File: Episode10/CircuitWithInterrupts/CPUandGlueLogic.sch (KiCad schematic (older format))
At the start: 27 parts, among them SW100 SW_Push, U100 74HCT245, U101 74HCT245, U102 MAX708, U103 HD6809, U104 74HCT245, U105 74HCT365, U106 74HCT00, U107 74HCT27, U108 74HCT138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

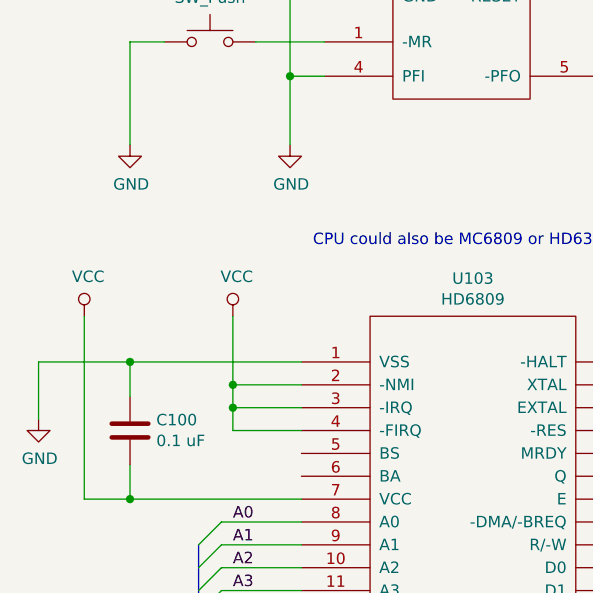
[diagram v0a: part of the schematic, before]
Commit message: integrated interrupt controller
Added ~IRQ input to core module, and changed the
wiring of the CPU's ~IRQ input to feed in the ~IRQ
output of the interrupt controller.  (A pull-up
resistor will keep this input high when the interrupt
controller isn't installed.)

Have the peripheral module send the Timer 1 output
to the interrupt controller's ~IRQ3 input.  This will
be the system periodic timer interrupt.

Also have the peripheral module export the pins of
Port C, and use PC0 and PC1 to clear the flip flops
that latch a pulse on ~IRQ3 and ~IRQ6, which are
edge-triggered.
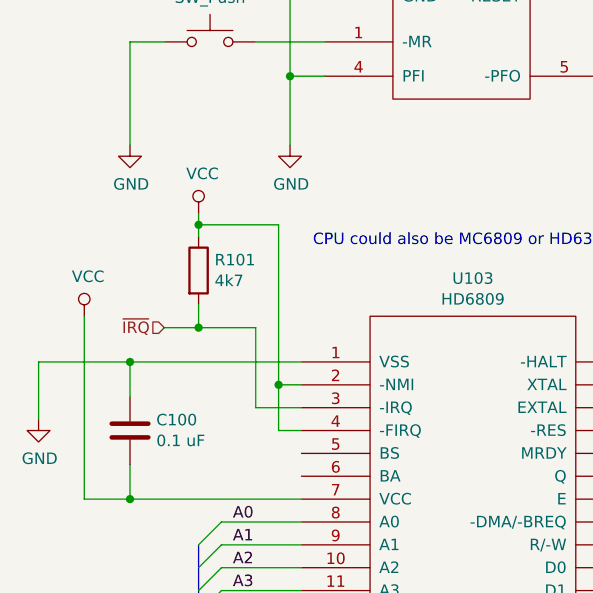
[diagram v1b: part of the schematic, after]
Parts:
- added R101: 4k7, symbol device:R
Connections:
- net labels added: ~IRQ
- wire segments 322 -> 328
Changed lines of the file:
@@
 $EndComp
 Wire Wire Line
-	1800 3750 1500 3750
-Wire Wire Line
-	1500 3750 1500 3650
-$Comp
-L power:VCC #PWR0105
-U 1 1 5CFA91DE
-P 1500 3250
-F 0 "#PWR0105" H 1500 3100 50  0001 C CNN
-F 1 "VCC" H 1517 3423 50  0000 C CNN
-F 2 "" H 1500 3250 50  0001 C CNN
-F 3 "" H 1500 3250 50  0001 C CNN
-	1    1500 3250
-	1    0    0    -1
-$EndComp
+	1800 3750 1700 3750
 Wire Wire Line
 	3300 3650 4350 3650
@@
 Connection ~ 4350 3150
 Wire Wire Line
-	1800 3650 1500 3650
-Connection ~ 1500 3650
-Wire Wire Line
-	1500 3650 1500 3550
-Wire Wire Line
-	1800 3550 1500 3550
-Connection ~ 1500 3550
-Wire Wire Line
-	1500 3550 1500 3250
+	1800 3550 1700 3550
+Connection ~ 1700 3550
 Text Notes 4000 2800 0    50   ~ 0
 Crystal frequency should be between 2 and 4 MHz.\nI used 3.6864 MHz.
@@
 Text HLabel 6850 7150 2    50   Output ~ 0
 R~W
+Wire Wire Line
+	1700 3550 1700 3750
+Wire Wire Line
+	1800 3650 1600 3650
+Wire Wire Line
+	1600 3650 1600 3300
+Wire Wire Line
+	1600 3300 1350 3300
+Text HLabel 1200 3300 0    50   Input ~ 0
+~IRQ
+$Comp
+L device:R R101
+U 1 1 5E301027
+P 1350 3050
+F 0 "R101" H 1420 3096 50  0000 L CNN
+F 1 "4k7" H 1420 3005 50  0000 L CNN
+F 2 "" V 1280 3050 50  0001 C CNN
+F 3 "" H 1350 3050 50  0001 C CNN
+	1    1350 3050
+	1    0    0    -1
+$EndComp
+Wire Wire Line
+	1350 3200 1350 3300
+Connection ~ 1350 3300
+Wire Wire Line
+	1350 3300 1200 3300
+Wire Wire Line
+	1350 2900 1350 2850
+$Comp
+L power:VCC #PWR?
+U 1 1 5E36696F
+P 1350 2800
+F 0 "#PWR?" H 1350 2650 50  0001 C CNN
+F 1 "VCC" H 1367 2973 50  0000 C CNN
+F 2 "" H 1350 2800 50  0001 C CNN
+F 3 "" H 1350 2800 50  0001 C CNN
+	1    1350 2800
+	1    0    0    -1
+$EndComp
+Wire Wire Line
+	1700 2850 1350 2850
+Wire Wire Line
+	1700 2850 1700 3550
+Connection ~ 1350 2850
+Wire Wire Line
+	1350 2850 1350 2800
 Wire Bus Line
-	1000 5700 3650 5700
+	2450 6150 2450 9200
+Wire Bus Line
+	4500 4450 4500 7250
+Wire Bus Line
+	1350 4250 1350 5600
 Wire Bus Line
 	3750 5250 3750 5600
 Wire Bus Line
-	1350 4250 1350 5600
-Wire Bus Line
-	4500 4450 4500 7250
-Wire Bus Line
-	2450 6150 2450 9200
+	1000 5700 3650 5700
 $EndSCHEMATC

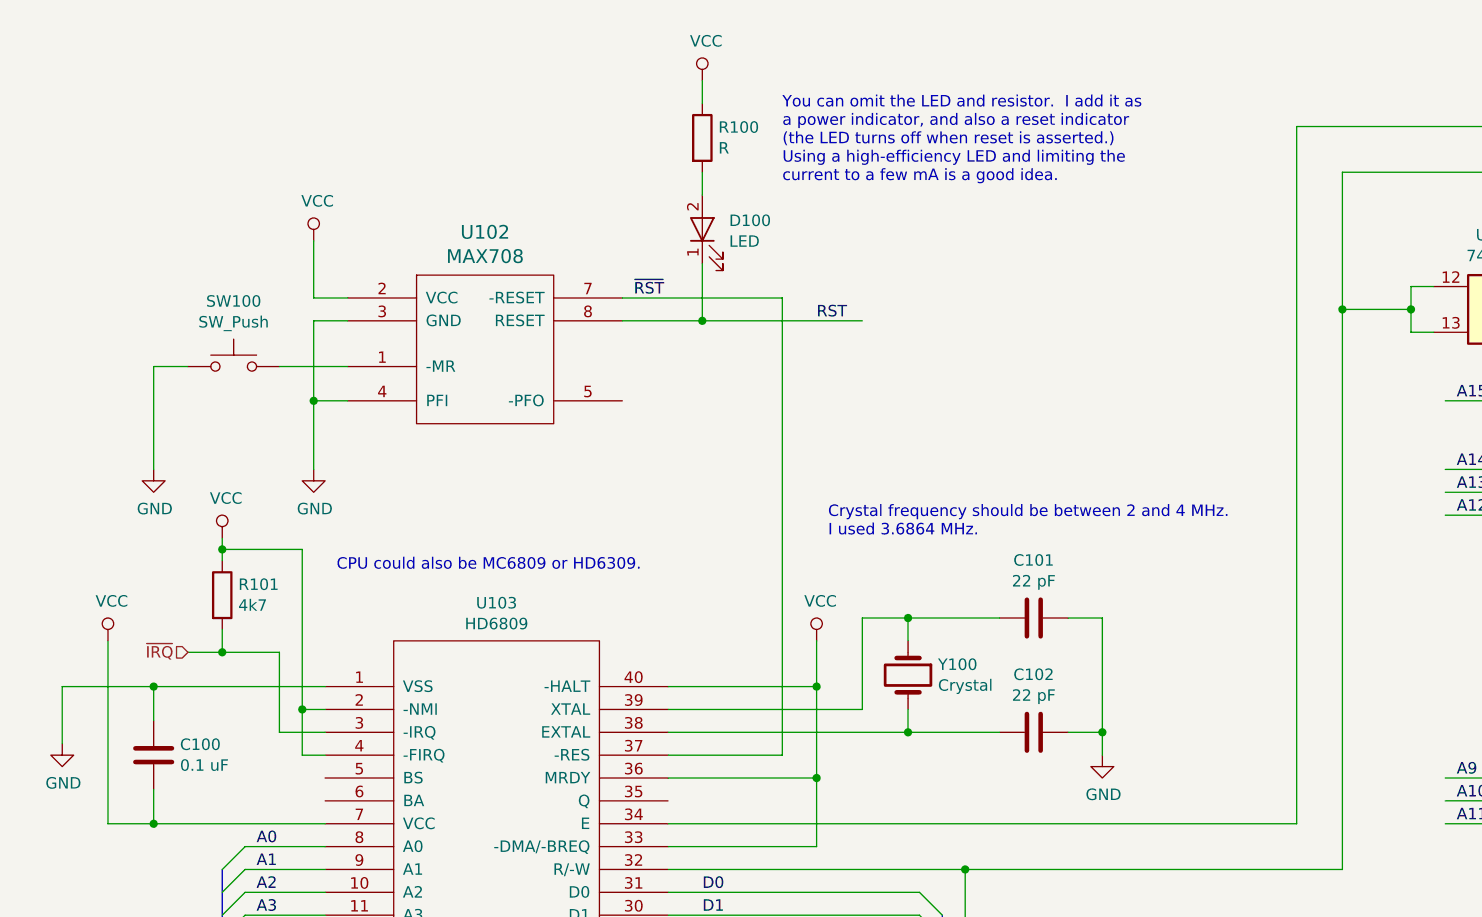
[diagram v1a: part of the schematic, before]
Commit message: add pull-ups to -IRQ, -FIRQ, and -NMI
This allows them to be driven low if used, but still
works if they are not explicitly driven.
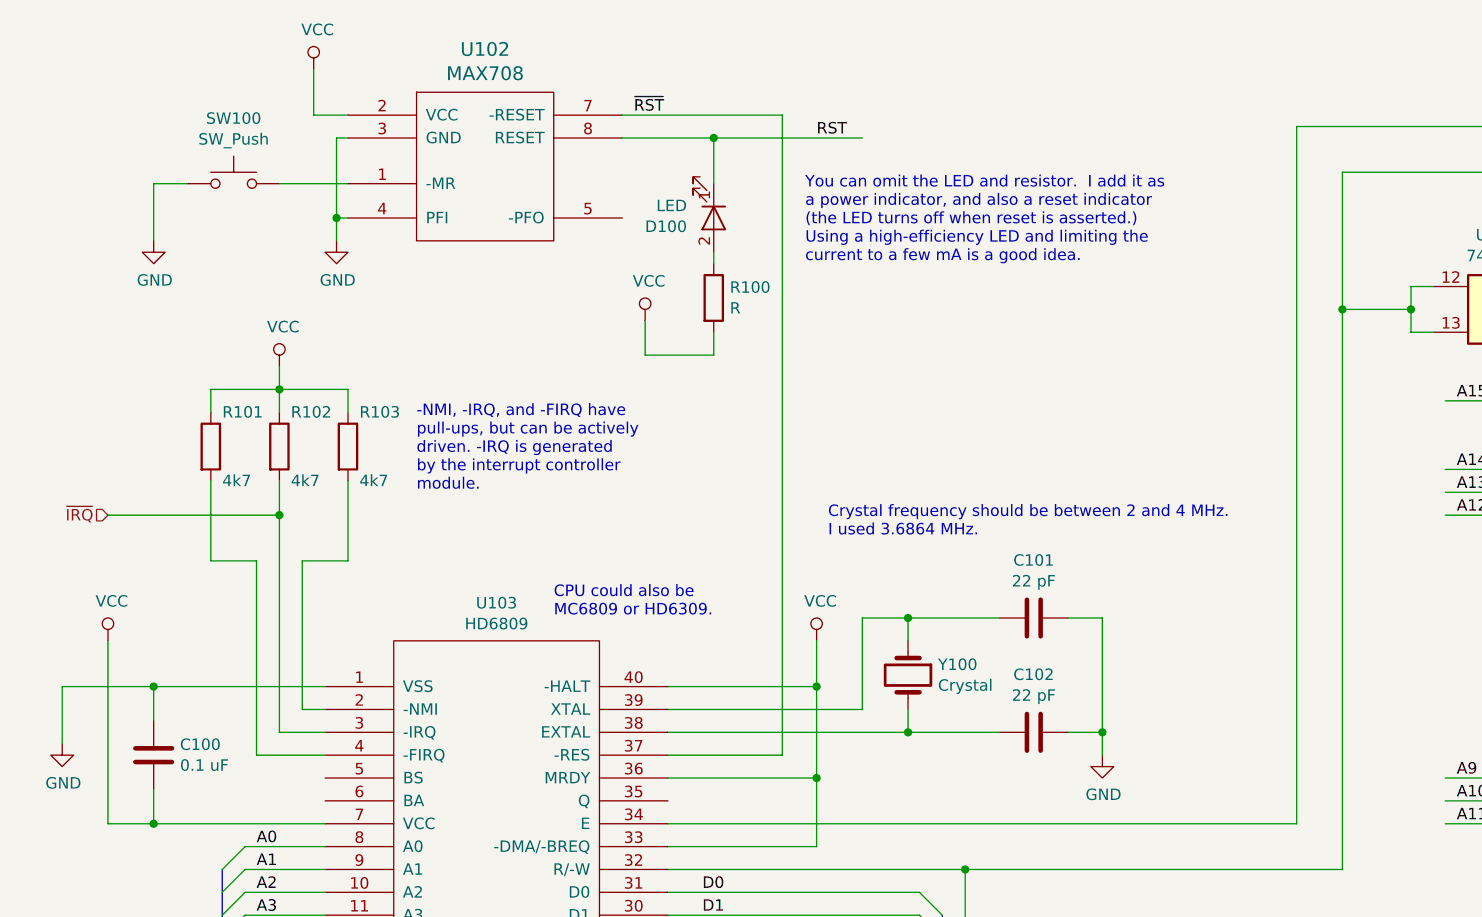
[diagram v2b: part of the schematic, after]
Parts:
- added R102, R103: 4k7, symbol device:R
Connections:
- wire segments 328 -> 336
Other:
- note added: "-NMI, -IRQ, and -FIRQ have\npull-ups, but can be actively\ndriven. -IRQ is generated\nby the interrupt controller\nmodule."
- note added: "CPU could also be\nMC6809 or HD6309."
- note removed: "CPU could also be MC6809 or HD6309."
- moved on the sheet: D100, R100, R101, SW100, U102
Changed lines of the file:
@@
 L ya68k:MAX708 U102
 U 1 1 5CFA9144
-P 2500 1950
-F 0 "U102" H 2500 2437 60  0000 C CNN
-F 1 "MAX708" H 2500 2331 60  0000 C CNN
-F 2 "" H 2500 1950 60  0000 C CNN
-F 3 "" H 2500 1950 60  0000 C CNN
-	1    2500 1950
+P 2500 1150
+F 0 "U102" H 2500 1637 60  0000 C CNN
+F 1 "MAX708" H 2500 1531 60  0000 C CNN
+F 2 "" H 2500 1150 60  0000 C CNN
+F 3 "" H 2500 1150 60  0000 C CNN
+	1    2500 1150
 	1    0    0    -1
 $EndComp
@@
 L Switch:SW_Push SW100
 U 1 1 5CFA914B
-P 1400 2050
-F 0 "SW100" H 1400 2335 50  0000 C CNN
-F 1 "SW_Push" H 1400 2244 50  0000 C CNN
-F 2 "" H 1400 2250 50  0001 C CNN
-F 3 "" H 1400 2250 50  0001 C CNN
-	1    1400 2050
-	1    0    0    -1
-$EndComp
-Wire Wire Line
-	1900 1750 1750 1750
-Wire Wire Line
-	1750 1750 1750 1500
+P 1400 1250
+F 0 "SW100" H 1400 1535 50  0000 C CNN
+F 1 "SW_Push" H 1400 1444 50  0000 C CNN
+F 2 "" H 1400 1450 50  0001 C CNN
+F 3 "" H 1400 1450 50  0001 C CNN
+	1    1400 1250
+	1    0    0    -1
+$EndComp
+Wire Wire Line
+	1900 950  1750 950
+Wire Wire Line
+	1750 950  1750 750
 $Comp
 L power:VCC #PWR0106
 U 1 1 5CFA9154
-P 1750 1500
-F 0 "#PWR0106" H 1750 1350 50  0001 C CNN
-F 1 "VCC" H 1767 1673 50  0000 C CNN
-F 2 "" H 1750 1500 50  0001 C CNN
-F 3 "" H 1750 1500 50  0001 C CNN
-	1    1750 1500
-	1    0    0    -1
-$EndComp
-Wire Wire Line
-	1900 1850 1750 1850
-Wire Wire Line
-	1750 1850 1750 2200
-Wire Wire Line
-	1900 2200 1750 2200
-Connection ~ 1750 2200
-Wire Wire Line
-	1750 2200 1750 2500
+P 1750 750
+F 0 "#PWR0106" H 1750 600 50  0001 C CNN
+F 1 "VCC" H 1767 923 50  0000 C CNN
+F 2 "" H 1750 750 50  0001 C CNN
+F 3 "" H 1750 750 50  0001 C CNN
+	1    1750 750
+	1    0    0    -1
+$EndComp
+Wire Wire Line
+	1900 1050 1850 1050
+Wire Wire Line
+	1850 1050 1850 1400
+Wire Wire Line
+	1900 1400 1850 1400
+Connection ~ 1850 1400
+Wire Wire Line
+	1850 1400 1850 1500
 $Comp
 L power:GND #PWR0107
 U 1 1 5CFA915F
-P 1750 2500
-F 0 "#PWR0107" H 1750 2250 50  0001 C CNN
-F 1 "GND" H 1755 2327 50  0000 C CNN
-F 2 "" H 1750 2500 50  0001 C CNN
-F 3 "" H 1750 2500 50  0001 C CNN
-	1    1750 2500
-	1    0    0    -1
-$EndComp
-Wire Wire Line
-	1900 2050 1600 2050
-Wire Wire Line
-	1200 2050 1050 2050
-Wire Wire Line
-	1050 2050 1050 2500
+P 1850 1500
+F 0 "#PWR0107" H 1850 1250 50  0001 C CNN
+F 1 "GND" H 1855 1327 50  0000 C CNN
+F 2 "" H 1850 1500 50  0001 C CNN
+F 3 "" H 1850 1500 50  0001 C CNN
+	1    1850 1500
+	1    0    0    -1
+$EndComp
+Wire Wire Line
+	1900 1250 1600 1250
+Wire Wire Line
+	1200 1250 1050 1250
+Wire Wire Line
+	1050 1250 1050 1500
 $Comp
 L power:GND #PWR0104
 U 1 1 5CFA9168
-P 1050 2500
-F 0 "#PWR0104" H 1050 2250 50  0001 C CNN
-F 1 "GND" H 1055 2327 50  0000 C CNN
-F 2 "" H 1050 2500 50  0001 C CNN
-F 3 "" H 1050 2500 50  0001 C CNN
-	1    1050 2500
+P 1050 1500
+F 0 "#PWR0104" H 1050 1250 50  0001 C CNN
+F 1 "GND" H 1055 1327 50  0000 C CNN
+F 2 "" H 1050 1500 50  0001 C CNN
+F 3 "" H 1050 1500 50  0001 C CNN
+	1    1050 1500
 	1    0    0    -1
 $EndComp
@@
 	3300 3750 3800 3750
 Wire Wire Line
-	3800 3750 3800 1750
-Wire Wire Line
-	3800 1750 3100 1750
+	3800 3750 3800 950
+Wire Wire Line
+	3800 950  3100 950
 $Comp
 L device:LED D100
 U 1 1 5CFA9178
-P 3450 1450
-F 0 "D100" V 3488 1333 50  0000 R CNN
-F 1 "LED" V 3397 1333 50  0000 R CNN
-F 2 "" H 3450 1450 50  0001 C CNN
-F 3 "" H 3450 1450 50  0001 C CNN
-	1    3450 1450
-	0    -1   -1   0
+P 3500 1400
+F 0 "D100" V 3538 1283 50  0000 R CNN
+F 1 "LED" V 3447 1283 50  0000 R CNN
+F 2 "" H 3500 1400 50  0001 C CNN
+F 3 "" H 3500 1400 50  0001 C CNN
+	1    3500 1400
+	0    1    1    0
 $EndComp
 $Comp
 L device:R R100
 U 1 1 5CFA917F
-P 3450 1050
-F 0 "R100" H 3520 1096 50  0000 L CNN
-F 1 "R" H 3520 1005 50  0000 L CNN
-F 2 "" V 3380 1050 50  0001 C CNN
-F 3 "" H 3450 1050 50  0001 C CNN
-	1    3450 1050
-	1    0    0    -1
-$EndComp
-Wire Wire Line
-	3450 1200 3450 1300
-Wire Wire Line
-	3450 1600 3450 1850
-Wire Wire Line
-	3450 1850 3100 1850
-Wire Wire Line
-	3450 900  3450 800
+P 3500 1750
+F 0 "R100" H 3570 1796 50  0000 L CNN
+F 1 "R" H 3570 1705 50  0000 L CNN
+F 2 "" V 3430 1750 50  0001 C CNN
+F 3 "" H 3500 1750 50  0001 C CNN
+	1    3500 1750
+	1    0    0    -1
+$EndComp
+Wire Wire Line
+	3500 1550 3500 1600
+Wire Wire Line
+	3500 1050 3500 1250
+Wire Wire Line
+	3500 1050 3100 1050
 $Comp
 L power:VCC #PWR0111
 U 1 1 5CFA918A
-P 3450 800
-F 0 "#PWR0111" H 3450 650 50  0001 C CNN
-F 1 "VCC" H 3467 973 50  0000 C CNN
-F 2 "" H 3450 800 50  0001 C CNN
-F 3 "" H 3450 800 50  0001 C CNN
-	1    3450 800
+P 3200 1850
+F 0 "#PWR0111" H 3200 1700 50  0001 C CNN
+F 1 "VCC" H 3217 2023 50  0000 C CNN
+F 2 "" H 3200 1850 50  0001 C CNN
+F 3 "" H 3200 1850 50  0001 C CNN
+	1    3200 1850
 	1    0    0    -1
 $EndComp
@@
 $EndComp
 Wire Wire Line
-	1800 3750 1700 3750
-Wire Wire Line
 	3300 3650 4350 3650
 Connection ~ 4350 3650
@@
 	4150 3550 3300 3550
 Connection ~ 4350 3150
-Wire Wire Line
-	1800 3550 1700 3550
-Connection ~ 1700 3550
 Text Notes 4000 2800 0    50   ~ 0
 Crystal frequency should be between 2 and 4 MHz.\nI used 3.6864 MHz.
-Text Notes 3800 1250 0    50   ~ 0
+Text Notes 3900 1600 0    50   ~ 0
 You can omit the LED and resistor.  I add it as\na power indicator, and also a reset indicator\n(the LED turns off when reset is asserted.)\nUsing a high-efficiency LED and limiting the\ncurrent to a few mA is a good idea.
-Text Notes 1850 2950 0    50   ~ 0
-CPU could also be MC6809 or HD6309.
+Text Notes 2800 3150 0    50   ~ 0
+CPU could also be\nMC6809 or HD6309.
 Wire Wire Line
 	3300 3850 3950 3850
@@
 Text HLabel 6850 6850 2    50   Output ~ 0
 ~WMEM~
-Text Label 3150 1750 0    50   ~ 0
+Text Label 3150 950  0    50   ~ 0
 ~RST~
 Text Label 5350 7050 0    50   ~ 0
@@
 Text HLabel 6850 6950 2    50   Output ~ 0
 ~RST~
-Text Label 3950 1850 0    50   ~ 0
+Text Label 3950 1050 0    50   ~ 0
 RST
 Text Notes 5700 7950 0    50   ~ 0
@@
 Place C108-C111 near the\npower pins of U100, U101, U104, U105
 Wire Wire Line
-	4150 1850 3450 1850
-Connection ~ 3450 1850
+	4150 1050 3500 1050
+Connection ~ 3500 1050
 Text HLabel 10350 2600 2    50   Output ~ 0
 ~ROMEN~
@@
 Text HLabel 6850 7150 2    50   Output ~ 0
 R~W
-Wire Wire Line
-	1700 3550 1700 3750
-Wire Wire Line
-	1800 3650 1600 3650
-Wire Wire Line
-	1600 3650 1600 3300
-Wire Wire Line
-	1600 3300 1350 3300
-Text HLabel 1200 3300 0    50   Input ~ 0
+Text HLabel 850  2700 0    50   Input ~ 0
 ~IRQ
 $Comp
 L device:R R101
 U 1 1 5E301027
-P 1350 3050
-F 0 "R101" H 1420 3096 50  0000 L CNN
-F 1 "4k7" H 1420 3005 50  0000 L CNN
-F 2 "" V 1280 3050 50  0001 C CNN
-F 3 "" H 1350 3050 50  0001 C CNN
-	1    1350 3050
-	1    0    0    -1
-$EndComp
-Wire Wire Line
-	1350 3200 1350 3300
-Connection ~ 1350 3300
-Wire Wire Line
-	1350 3300 1200 3300
-Wire Wire Line
-	1350 2900 1350 2850
+P 1300 2400
+F 0 "R101" H 1350 2550 50  0000 L CNN
+F 1 "4k7" H 1350 2250 50  0000 L CNN
+F 2 "" V 1230 2400 50  0001 C CNN
+F 3 "" H 1300 2400 50  0001 C CNN
+	1    1300 2400
+	1    0    0    -1
+$EndComp
 $Comp
 L power:VCC #PWR?
 U 1 1 5E36696F
-P 1350 2800
-F 0 "#PWR?" H 1350 2650 50  0001 C CNN
-F 1 "VCC" H 1367 2973 50  0000 C CNN
-F 2 "" H 1350 2800 50  0001 C CNN
-F 3 "" H 1350 2800 50  0001 C CNN
-	1    1350 2800
-	1    0    0    -1
-$EndComp
-Wire Wire Line
-	1700 2850 1350 2850
-Wire Wire Line
-	1700 2850 1700 3550
-Connection ~ 1350 2850
-Wire Wire Line
-	1350 2850 1350 2800
+P 1600 2050
+F 0 "#PWR?" H 1600 1900 50  0001 C CNN
+F 1 "VCC" H 1617 2223 50  0000 C CNN
+F 2 "" H 1600 2050 50  0001 C CNN
+F 3 "" H 1600 2050 50  0001 C CNN
+	1    1600 2050
+	1    0    0    -1
+$EndComp
+$Comp
+L device:R R102
+U 1 1 5E71B466
+P 1600 2400
+F 0 "R102" H 1650 2550 50  0000 L CNN
+F 1 "4k7" H 1650 2250 50  0000 L CNN
+F 2 "" V 1530 2400 50  0001 C CNN
+F 3 "" H 1600 2400 50  0001 C CNN
+	1    1600 2400
+	1    0    0    -1
+$EndComp
+$Comp
+L device:R R103
+U 1 1 5E73C96F
+P 1900 2400
+F 0 "R103" H 1950 2550 50  0000 L CNN
+F 1 "4k7" H 1950 2250 50  0000 L CNN
+F 2 "" V 1830 2400 50  0001 C CNN
+F 3 "" H 1900 2400 50  0001 C CNN
+	1    1900 2400
+	1    0    0    -1
+$EndComp
+Wire Wire Line
+	1300 2250 1300 2150
+Wire Wire Line
+	1300 2150 1600 2150
+Wire Wire Line
+	1900 2150 1900 2250
+Wire Wire Line
+	1600 2050 1600 2150
+Connection ~ 1600 2150
+Wire Wire Line
+	1600 2150 1900 2150
+Wire Wire Line
+	1600 2250 1600 2150
+Wire Wire Line
+	3500 1900 3500 2000
+Wire Wire Line
+	3500 2000 3200 2000
+Wire Wire Line
+	3200 1850 3200 2000
+Wire Wire Line
+	1800 3550 1700 3550
+Wire Wire Line
+	1700 3550 1700 2900
+Wire Wire Line
+	1700 2900 1900 2900
+Wire Wire Line
+	1900 2900 1900 2550
+Wire Wire Line
+	1600 3650 1600 2700
+Wire Wire Line
+	1600 3650 1800 3650
+Wire Wire Line
+	1500 3750 1500 2900
+Wire Wire Line
+	1500 2900 1300 2900
+Wire Wire Line
+	1300 2900 1300 2550
+Wire Wire Line
+	1500 3750 1800 3750
+Wire Wire Line
+	850  2700 1600 2700
+Connection ~ 1600 2700
+Wire Wire Line
+	1600 2700 1600 2550
 Wire Bus Line
-	2450 6150 2450 9200
+	1000 5700 3650 5700
+Wire Bus Line
+	3750 5250 3750 5600
+Wire Bus Line
+	1350 4250 1350 5600
 Wire Bus Line
 	4500 4450 4500 7250
 Wire Bus Line
-	1350 4250 1350 5600
-Wire Bus Line
-	3750 5250 3750 5600
-Wire Bus Line
-	1000 5700 3650 5700
+	2450 6150 2450 9200
+Text Notes 2200 2600 0    50   ~ 0
+-NMI, -IRQ, and -FIRQ have\npull-ups, but can be actively\ndriven. -IRQ is generated\nby the interrupt controller\nmodule.
 $EndSCHEMATC
